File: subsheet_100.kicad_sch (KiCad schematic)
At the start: 21 parts, among them Q01 16MHz

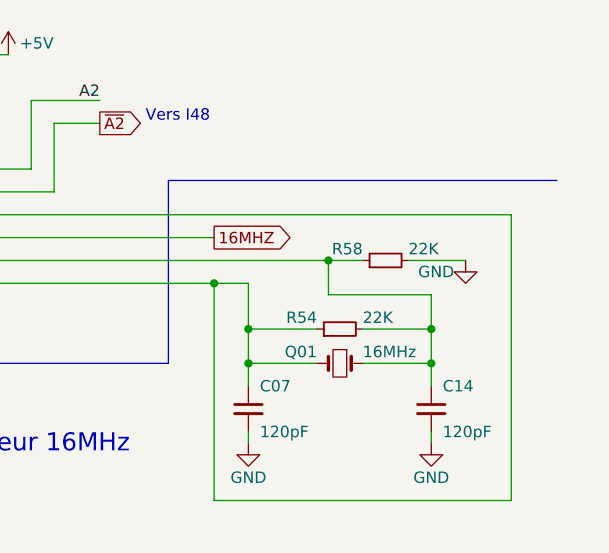
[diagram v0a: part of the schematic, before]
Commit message: #7 [bad value] R54 and R58 are 2K2, not 22K -- schematic
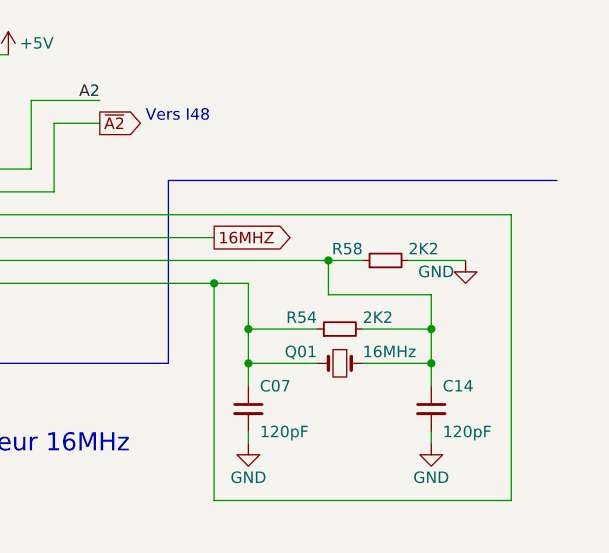
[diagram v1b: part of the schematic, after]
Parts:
- R54, R58: value 22K -> 2K2
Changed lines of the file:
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@@
       (effects (font (size 1.27 1.27)) (justify left))
     )
-    (property "Value" "22K" (at 171.45 224.79 90)
+    (property "Value" "2K2" (at 171.45 224.79 90)
       (effects (font (size 1.27 1.27)) (justify right))
     )
@@
       (effects (font (size 1.27 1.27)) (justify left))
     )
-    (property "Value" "22K" (at 176.53 217.17 90)
-      (effects (font (size 1.27 1.27)) (justify right))
-    )
+    (property "Value" "2K2" (at 176.53 217.17 90)
+      (effects (font (size 1.27 1.27)) (justify right))
+    )

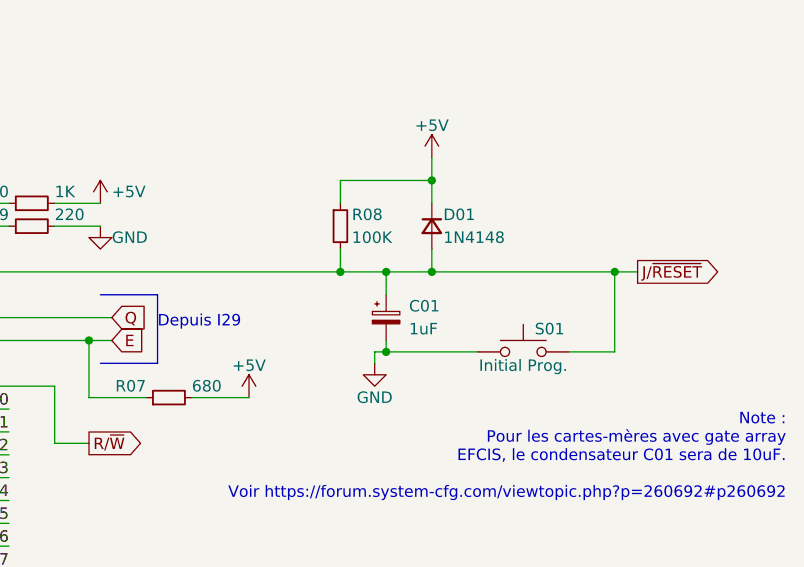
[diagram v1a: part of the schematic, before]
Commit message: subsheet_100 -- change values of C01, R08
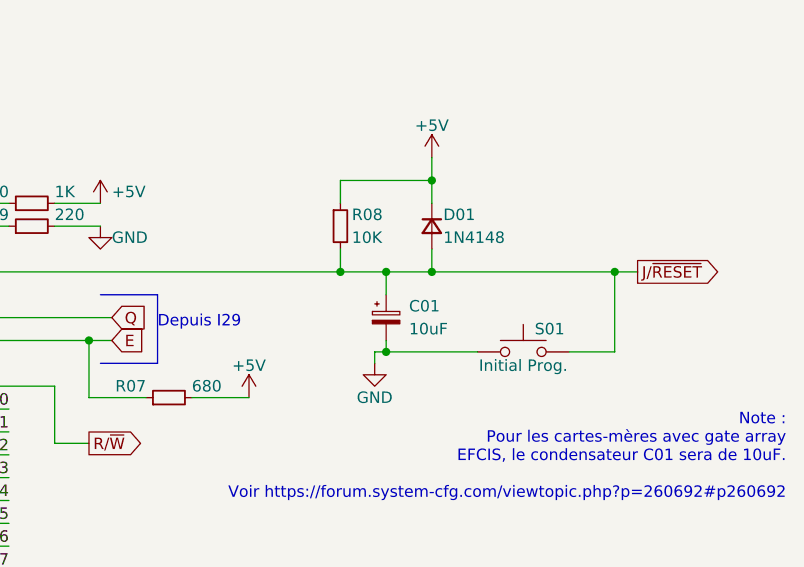
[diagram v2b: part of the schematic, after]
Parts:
- C01: value 1uF -> 10uF
- R08: value 100K -> 10K
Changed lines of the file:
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@@
       (effects (font (size 1.27 1.27)) (justify left))
     )
-    (property "Value" "1uF" (at 154.94 63.5 0)
+    (property "Value" "10uF" (at 154.94 63.5 0)
       (effects (font (size 1.27 1.27)) (justify left))
     )
@@
       (effects (font (size 1.27 1.27)) (justify left))
     )
-    (property "Value" "100K" (at 148.59 53.34 0)
+    (property "Value" "10K" (at 148.59 53.34 0)
       (effects (font (size 1.27 1.27)) (justify left))
     )

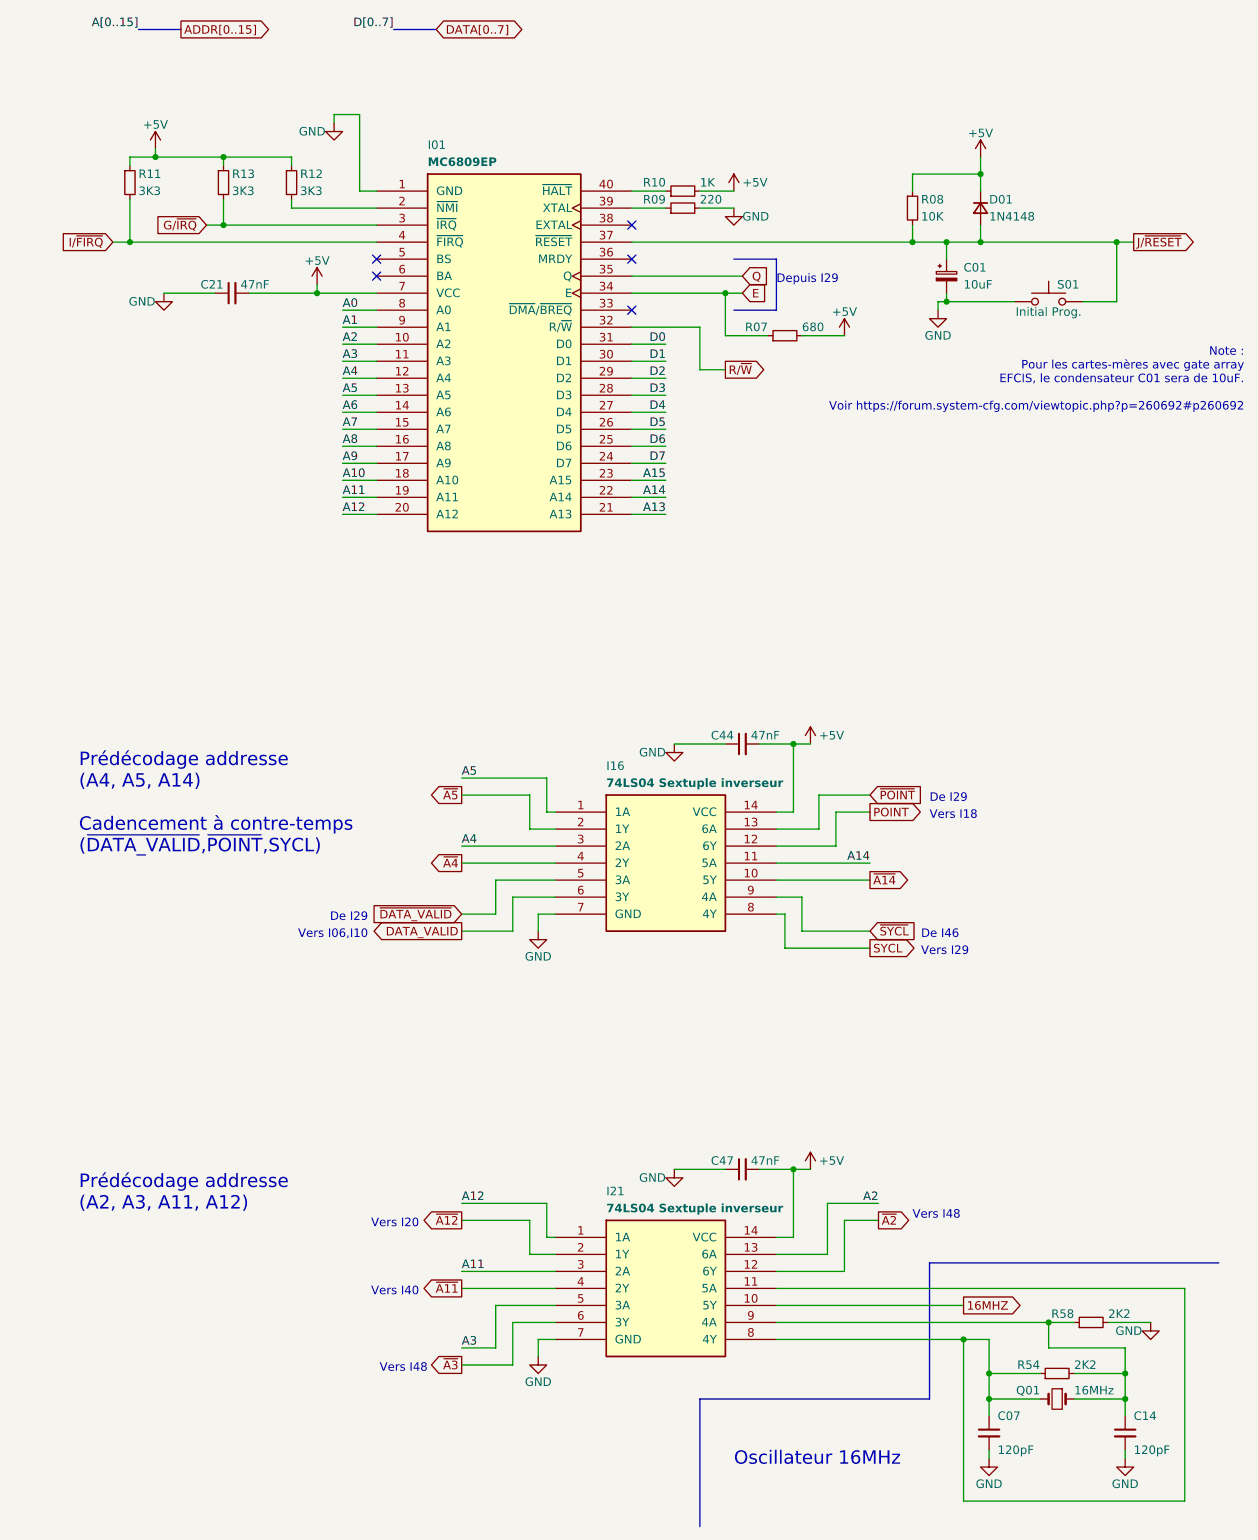
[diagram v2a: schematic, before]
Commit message: Resolves #11 : [ga efcis][schematics] Rewire I16 and I21
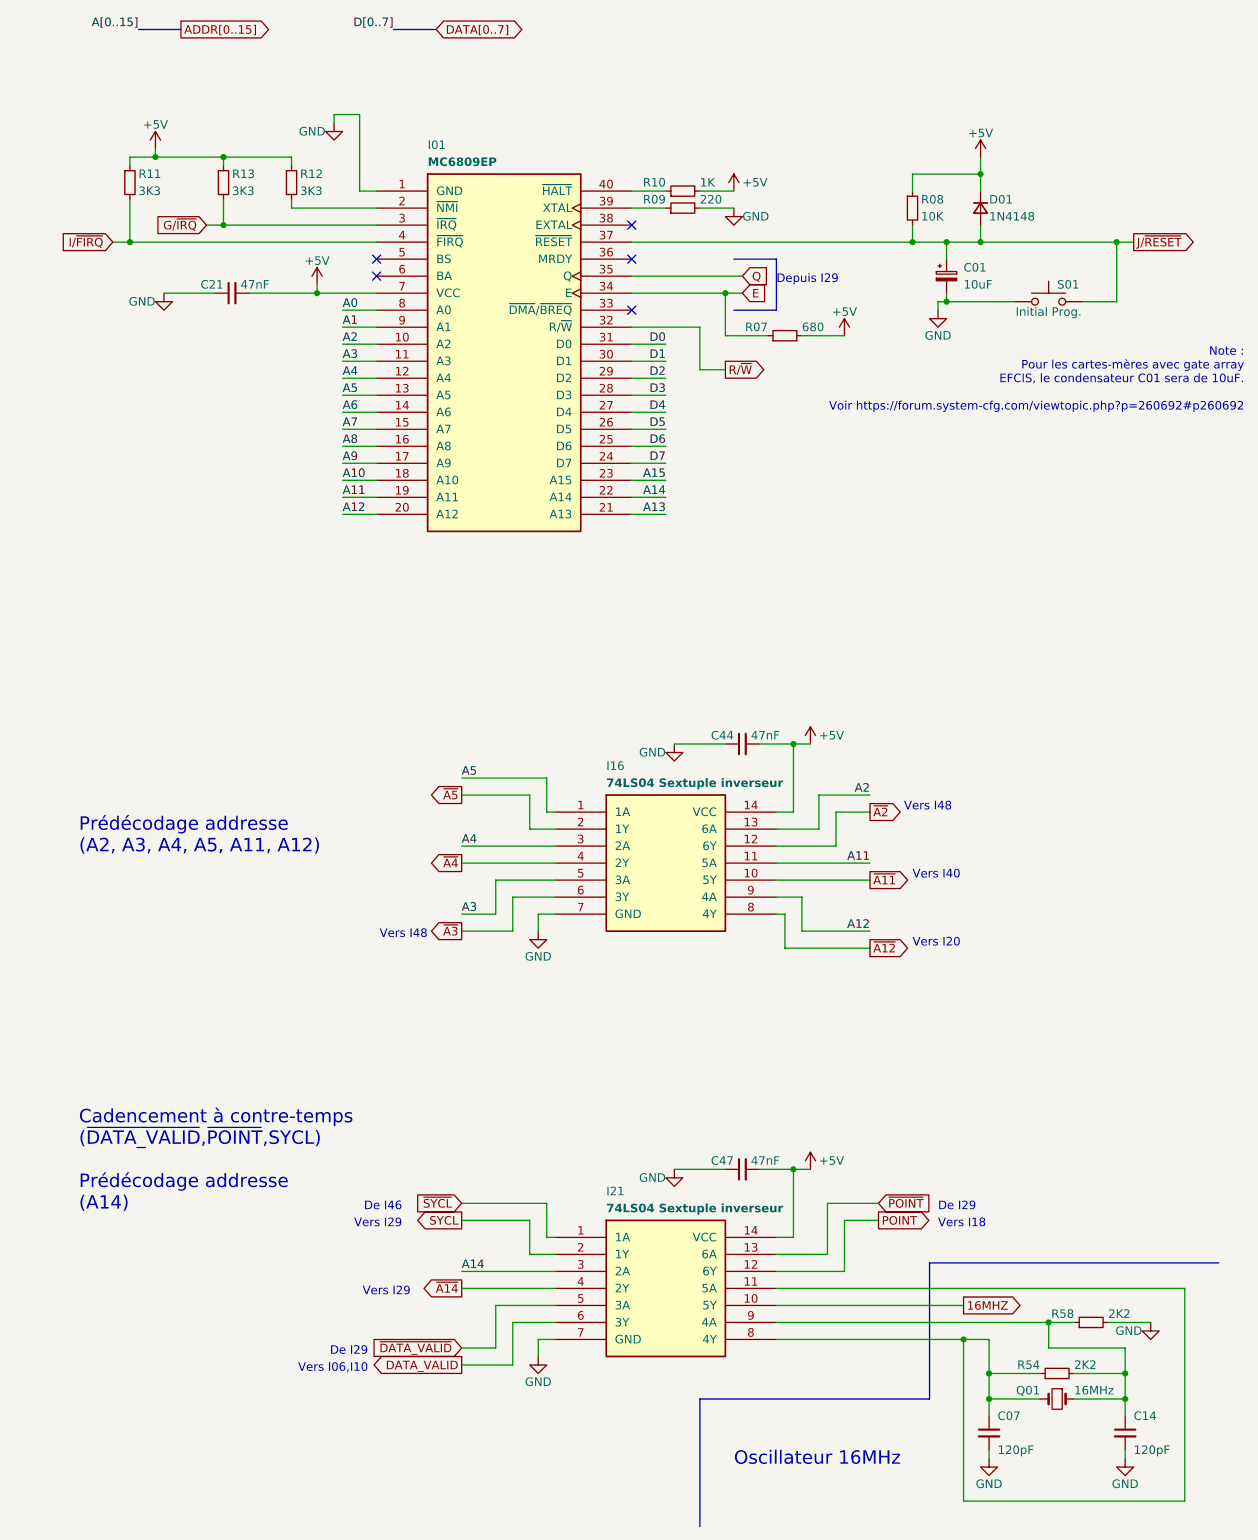
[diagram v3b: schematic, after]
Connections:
- net A11: now also I16.11 (5A); no longer I21.3 (2A)
- net A12: now also I16.9 (4A); no longer I21.1 (1A)
- net A14: now also I21.3 (2A); no longer I16.11 (5A)
- net A2: now also I16.13 (6A); no longer I21.13 (6A)
- net A3: now also I16.5 (3A); no longer I21.5 (3A)
- net DATA_VALID: now also I21.6 (3Y); no longer I16.6 (3Y)
- net POINT: now also I21.12 (6Y); no longer I16.12 (6Y)
- net SYCL: now also I21.2 (1Y); no longer I16.8 (4Y)
- net ~{A11}: now also I16.10 (5Y); no longer I21.4 (2Y)
- net ~{A12}: now also I16.8 (4Y); no longer I21.2 (1Y)
- net ~{A14}: now also I21.4 (2Y); no longer I16.10 (5Y)
- net ~{A2}: now also I16.12 (6Y); no longer I21.12 (6Y)
- net ~{A3}: now also I16.6 (3Y); no longer I21.6 (3Y)
- net ~{DATA_VALID}: now also I21.5 (3A); no longer I16.5 (3A)
- net ~{POINT}: now also I21.13 (6A); no longer I16.13 (6A)
- net ~{SYCL}: now also I21.1 (1A); no longer I16.9 (4A)
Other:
- note added: "Cadencement à contre-temps (~{DATA_VALID},~{POINT},SYCL) Prédécodage addresse (A14)"
- note added: "Prédécodage addresse (A2, A3, A4, A5, A11, A12)"
- note removed: "Prédécodage addresse (A2, A3, A11, A12)"
- note removed: "Prédécodage addresse (A4, A5, A14) Cadencement à contre-temps (~{DATA_VALID},~{POINT},SYCL)"

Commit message: update comments in cartridge
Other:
- title: Conversion du Thomson MO5 — Unité centrale v1 -> Conversion du Thomson MO5 — Unité centrale v2
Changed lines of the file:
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@@
   (paper "A4" portrait)
   (title_block
-    (title "Conversion du Thomson MO5 — Unité centrale v1")
-    (date "2024-12-30")
-    (rev "v1.0.0-rc2")
+    (title "Conversion du Thomson MO5 — Unité centrale v2")
+    (date "2025-02-08")
+    (rev "v2.0.0-alpha")
     (comment 1 "http://github.com/sporniket/kicad-conversions--thomson-mo5--v1")
-    (comment 3 "Gate Array Motorola MCA 1300 ALS")
-    (comment 4 "Reference : POP5001 501994-01")
+    (comment 3 "Gate Array EFCIS")
   )
   (junction (at 119.38 64.77) (diameter 0) (color 0 0 0 0)
